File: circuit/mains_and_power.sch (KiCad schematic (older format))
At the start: 26 parts, among them J1 Screw_Terminal_01x10, U1 AQH3223, U2 AQH3223, U3 AQH3223, U4 MPM-05-12, U5 ICL7660, U6 AOZ1280CI

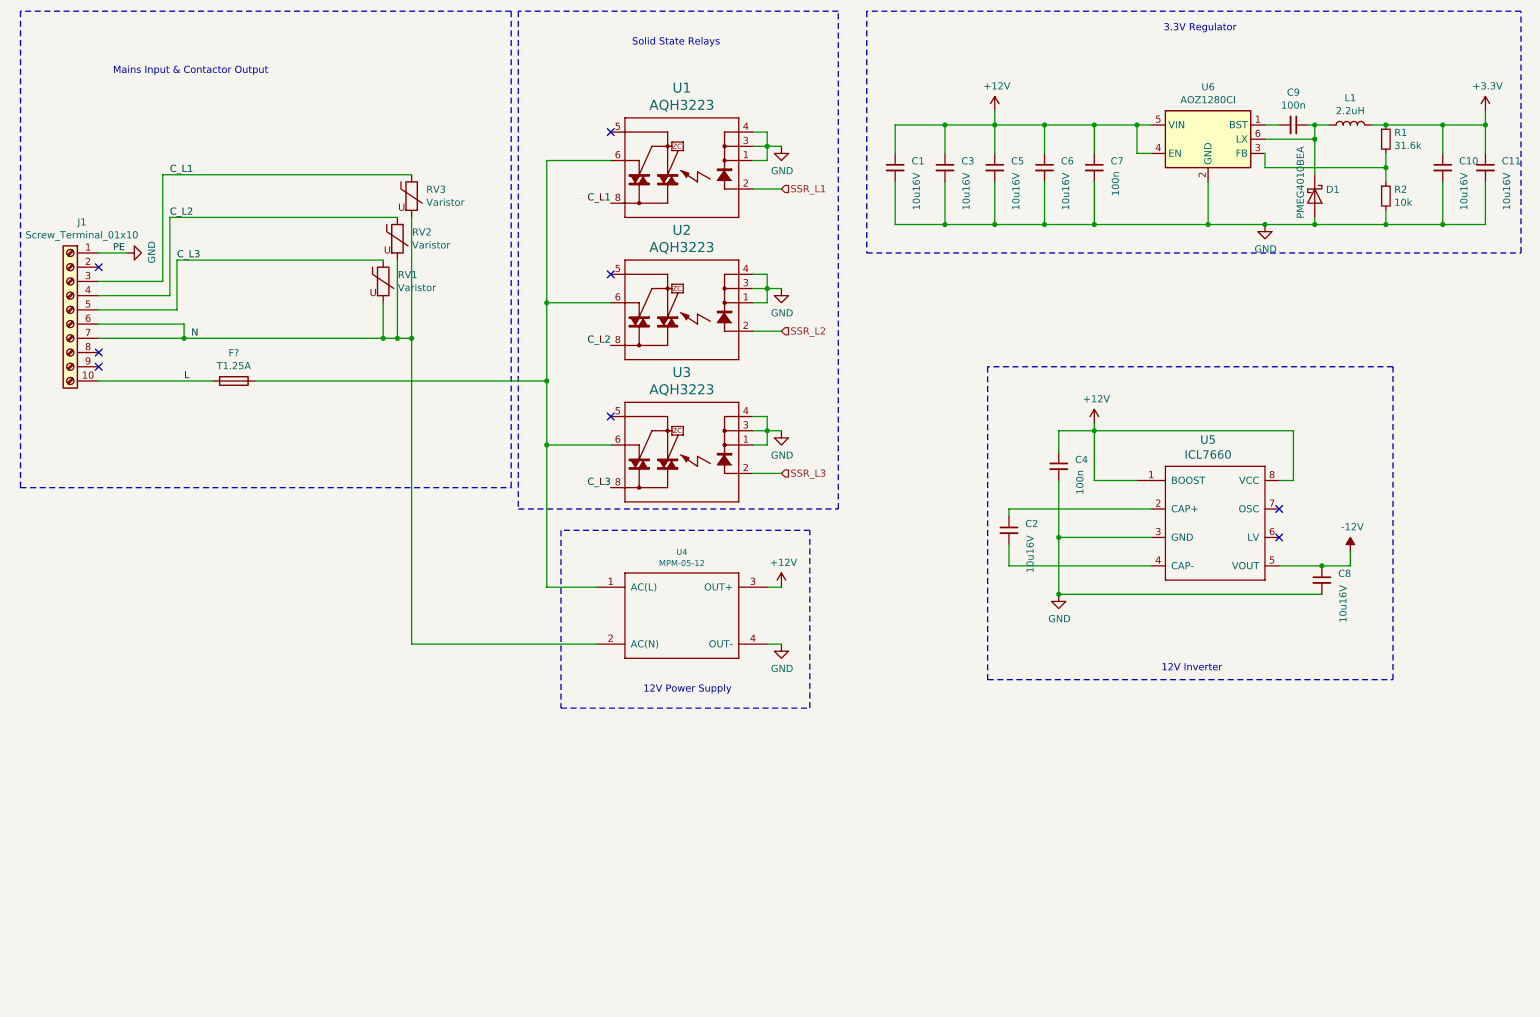
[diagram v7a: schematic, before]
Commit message: Update Parts List with Mouser ordering info
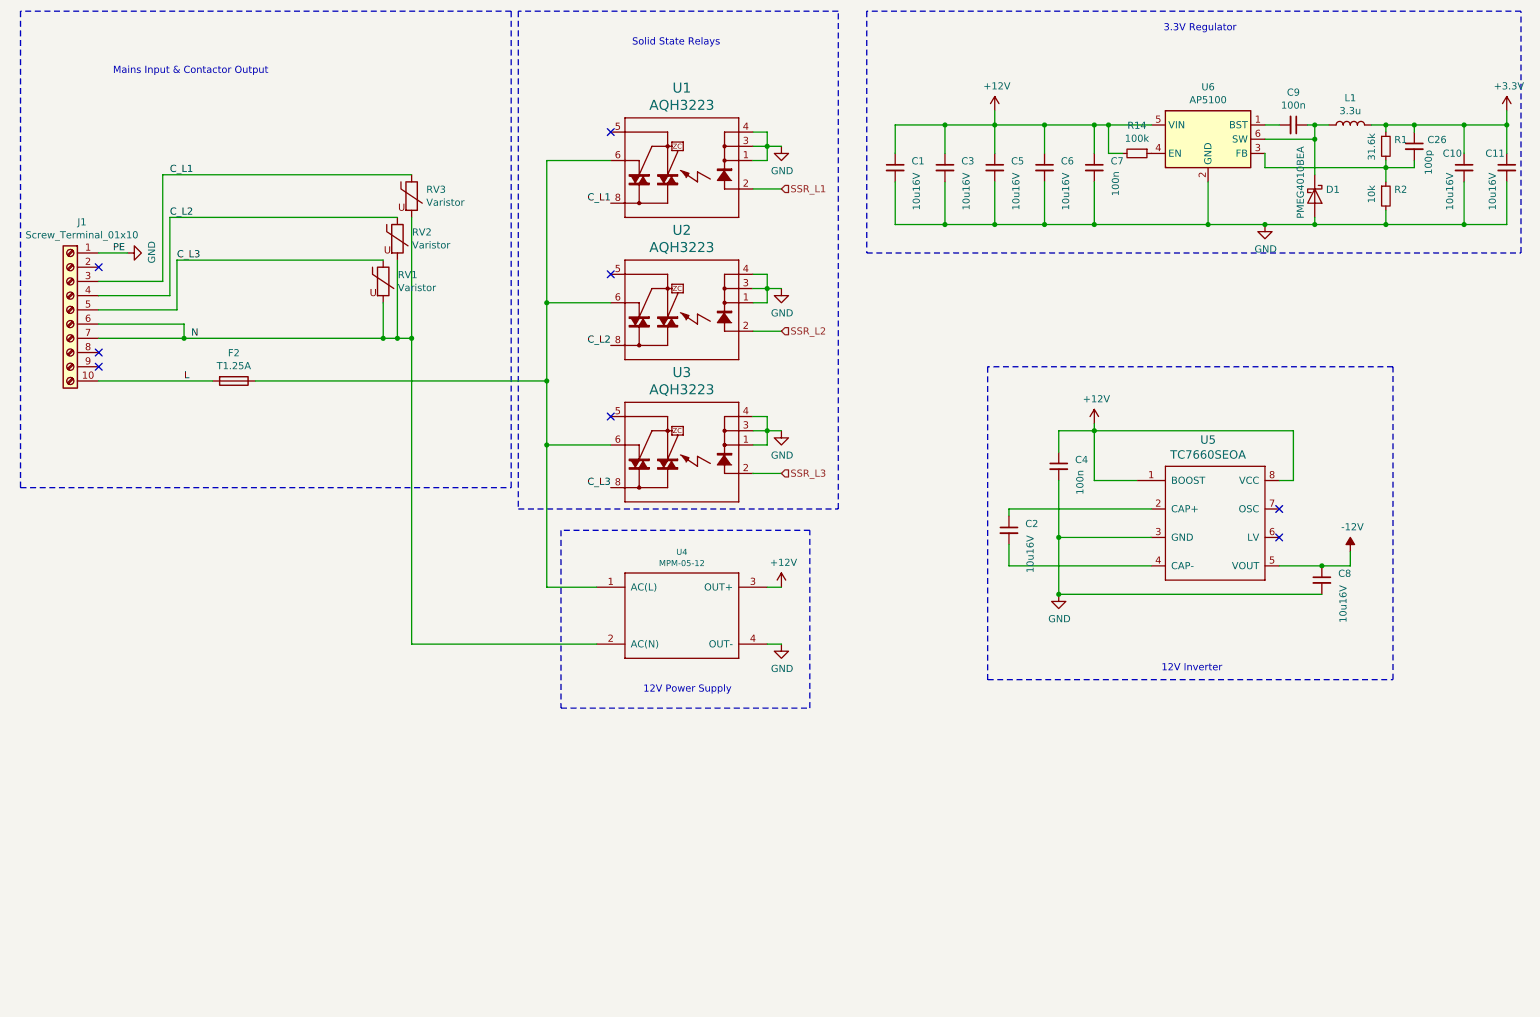
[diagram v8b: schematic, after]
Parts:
- removed U6: AOZ1280CI, Package_TO_SOT_SMD:SOT-23-6, symbol Regulator_Switching:AOZ1280CI
- added C26: 100p, symbol Device:C_Small
- added R14: 100k, Resistor_SMD:R_0603_1608Metric_Pad1.05x0.95mm_HandSolder, symbol Device:R_Small
- added U6: AP5100, Package_TO_SOT_SMD:SOT-23-6, symbol smartevse:AP5100
- C1, C10, C11, C2, C3, C5, C6, C8: Part Würth Elektronik WCAP-CSGP 885012107014 Keramik-Kondensator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 -> (none); PartNo 1278809 -> (none); Supplier Conrad -> Mouser
- C4, C7, C9: Part Kemet C0603C104K3RAC7867+ Keramik-Kondensator SMD 0603 100 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 -> (none); PartNo 1420339 -> (none); Supplier Conrad -> Mouser
- D1: Part Nexperia Schottky-Diode - Gleichrichter PMEG4010BEA,135 SOD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 -> (none); PartNo 1111813 -> 771-PMEG4010BEA,135; Supplier Conrad -> Mouser
- F2: renamed from F?; Part ESKA 883018 Kleinstsicherung radial bedrahtet eckig 1.25 A 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 -> (none); PartNo 524348 -> 576-3921125000; Supplier Conrad -> Mouser
- J1: PartNo (none) -> 651-1707111; Supplier (none) -> Mouser
- L1: value 2.2uH -> 3.3u; Part Würth Elektronik WE-GFH 744764902 HF-Drossel SMD 3225 2.2 µ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 -> (none); PartNo 1385329 -> 810-MLF1608A3R3J; Supplier Conrad -> Mouser
- R1: Part TRU COMPONENTS TC-0603SAJ0303T5E203 Dickschicht-Widerstand 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 -> (none); PartNo 1584281 -> 594-MCT06030C3162FP5; Supplier Conrad -> Mouser
- R2: Part TRU COMPONENTS TC-0603SAF1002T5E203 Dickschicht-Widerstand 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 -> (none); PartNo 1585269 -> 594-MCT06030C1002FP5; Supplier Conrad -> Mouser
- RV1, RV2, RV3: footprint Varistor:RV_Disc_D16.5mm_W6.7mm_P7.5mm -> Varistor:RV_Disc_D15.5mm_W5mm_P7.5mm; Part TDK S14K275 Scheiben-Varistor 430V -> (none); PartNo 500675 -> 871-B72214S0271K551; Supplier Conrad -> Mouser
- U1, U2, U3: footprint (none) -> smartevse-footprints:DIL07SMD; Part Panasonic Halbleiterrelais AQH3223 Sofortschaltend -> (none); PartNo 504887 -> (none); Supplier Conrad -> Mouser
- U4: footprint (none) -> Converter_ACDC:Converter_ACDC_MeanWell_IRM-05-xx_THT; Part Mean Well MPM-05-12 AC/DC-Printnetzteil 12 V/DC 0.42 A 5 W -> (none); PartNo 1838042 -> (none); Supplier Conrad -> Mouser
- U5: value ICL7660 -> TC7660SEOA; footprint (none) -> Package_SO:SOIC-8_3.9x4.9mm_P1.27mm; Part Maxim Integrated ICL7662CBA+ PMIC -> (none); PartNo 1123919 -> (none); Supplier Conrad -> Mouser
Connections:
- net +12V: now also R14.2, U6.5 (VIN)
- net +3V3: now also C26.1
- net GND: now also U6.2 (GND)
- net at C9.2: now also U6.1 (BST)
- net at R1.2, R2.1: now also C26.2, U6.3 (FB)
- net at C9.1, D1.1 (K), L1.1: now also U6.6 (SW)
- new net: R14.1, U6.4 (EN)
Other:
- moved on the sheet: C10, C11, R1
